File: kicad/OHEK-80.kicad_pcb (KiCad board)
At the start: 2 copper layers, 364.3 x 135.7 mm, 231 parts, among them J1 USB_C_Receptacle_USB2.0_16P, J2 Conn_01x04, J3 Conn_01x05, SW1 SW_Push, SW2 SW_Push, U1 AMS1117-3.3, U10 GH39FKSW, U11 GH39FKSW, U12 GH39FKSW, U13 GH39FKSW, U14 GH39FKSW, U15 GH39FKSW, U16 GH39FKSW, U17 GH39FKSW, U18 GH39FKSW, U19 GH39FKSW, U2 RP2040, U20 GH39FKSW, U21 GH39FKSW, U22 GH39FKSW, U23 GH39FKSW, U24 GH39FKSW, U25 GH39FKSW, U26 GH39FKSW, U27 GH39FKSW, U28 GH39FKSW, U29 GH39FKSW, U3 GH39FKSW, U30 GH39FKSW, U31 GH39FKSW, U32 GH39FKSW, U33 GH39FKSW, U34 GH39FKSW, U35 GH39FKSW, U36 GH39FKSW, U37 GH39FKSW, U38 GH39FKSW, U39 GH39FKSW, U4 GH39FKSW, U40 GH39FKSW, U41 GH39FKSW, U42 GH39FKSW, U43 GH39FKSW, U44 GH39FKSW, U45 GH39FKSW, U46 GH39FKSW, U47 GH39FKSW, U48 GH39FKSW, U49 GH39FKSW, U5 GH39FKSW, U50 GH39FKSW, U51 GH39FKSW, U52 GH39FKSW, U53 GH39FKSW, U54 GH39FKSW, U55 GH39FKSW, U56 GH39FKSW, U57 GH39FKSW, U58 GH39FKSW, U59 GH39FKSW, U6 GH39FKSW, U60 GH39FKSW, U61 GH39FKSW, U62 GH39FKSW, U63 GH39FKSW, U64 GH39FKSW, U65 GH39FKSW, U66 GH39FKSW, U67 GH39FKSW, U68 GH39FKSW, U69 GH39FKSW, U7 GH39FKSW, U70 GH39FKSW, U71 GH39FKSW, U72 GH39FKSW, U73 GH39FKSW, U74 GH39FKSW, U75 GH39FKSW, U76 GH39FKSW, U77 GH39FKSW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

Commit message: Removed J2 and cleaned up PCB a bit
I realized that daughterboard support is useless as Void Switches are entirely contactless so there is no use in gasket mounting the keyboard.
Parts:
- removed J2: Conn_01x04, Connector_JST:JST_PH_S4B-PH-K_1x04_P2.00mm_Horizontal
- moved F1 11.0 mm to (162.1, 101.7)
- moved R4 9.10 mm to (171.2, 99.0), turned to 0 degrees
- moved R5 6.63 mm to (171.2, 100.9), turned to 0 degrees
- moved SW2 3.67 mm to (179.7, 122.9), turned to 180 degrees
- moved C12 1.94 mm to (176.1, 118.4), turned to 180 degrees
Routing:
- net +3V3: track 288.6 -> 264.1 mm, vias 126 -> 123
- net GND: track 646.6 -> 626.1 mm
- net +5V: track 30.8 -> 16.1 mm, vias 2 -> 0
- net Net-(U2-USB_DM): track 17.1 -> 9.86 mm
- net Net-(U2-USB_DP): track 15.6 -> 9.83 mm
- net VBUS: track 22.4 -> 18.5 mm
- net D+: track 31.0 -> 28.5 mm
- net Net-(R7-Pad1): track 11.4 -> 10.6 mm
- net D-: track 27.7 -> 27.2 mm

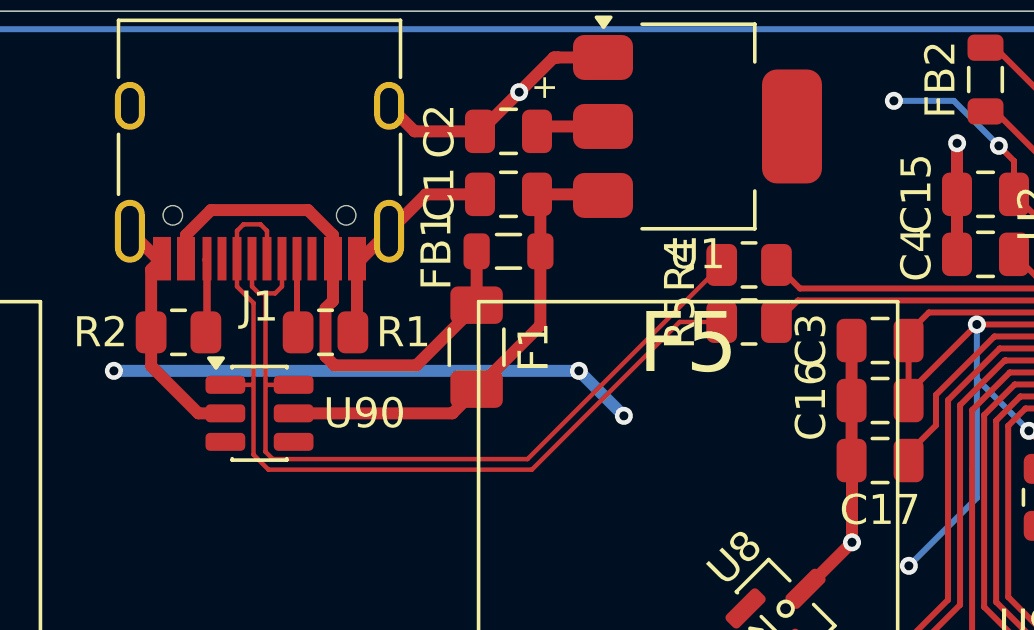
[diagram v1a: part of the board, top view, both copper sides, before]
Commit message: Fix issue where FB1 and F1 were in parallel
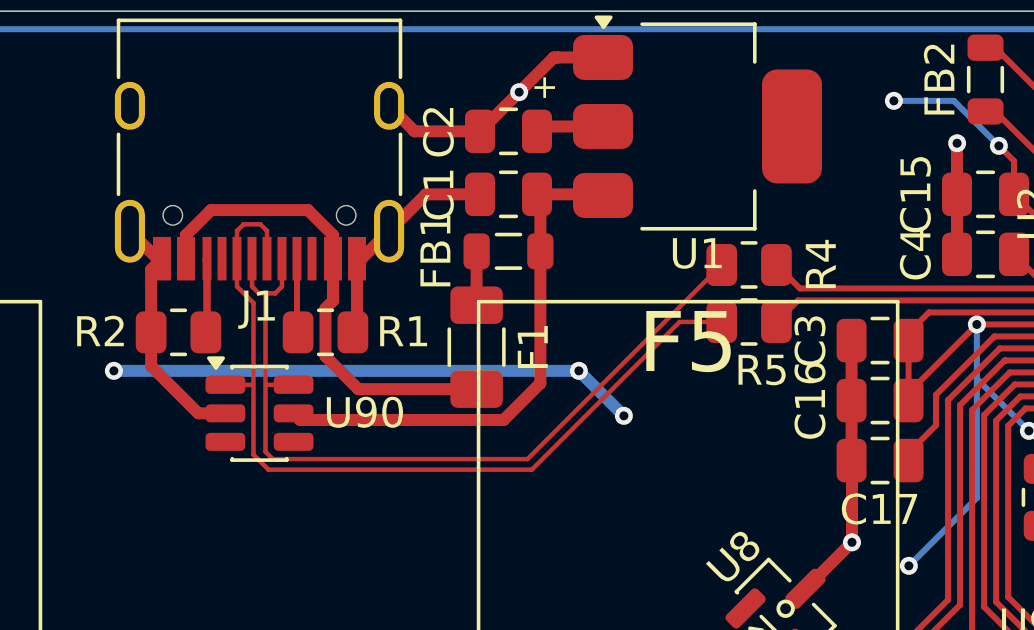
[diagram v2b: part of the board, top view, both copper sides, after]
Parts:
- C2: value 22u -> 22u Tantalum
- turned F1 to 90 degrees
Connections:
- F1 pad 2: +5V -> Net-(F1-Pad2)
- FB1 pad 1: VBUS -> Net-(F1-Pad2)
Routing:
- net VBUS: track 18.5 -> 16.2 mm
- net Net-(F1-Pad2): track 0.00 -> 1.80 mm
- net +5V: track 16.1 -> 17.4 mm

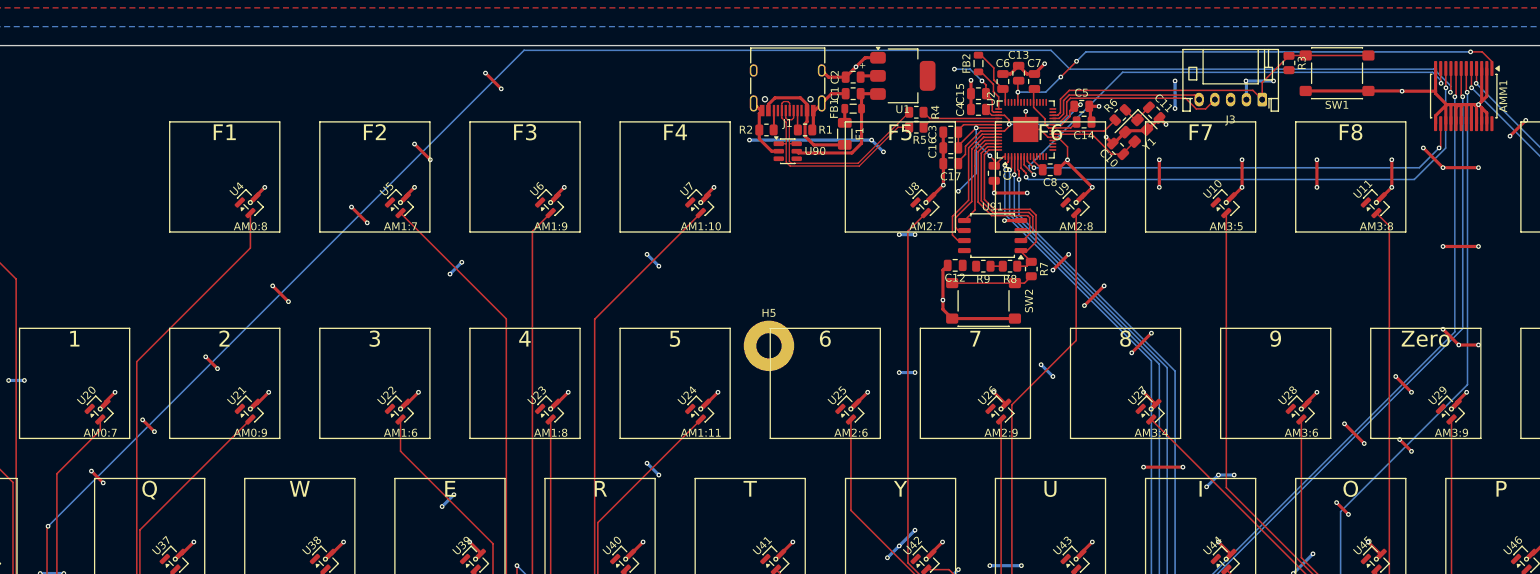
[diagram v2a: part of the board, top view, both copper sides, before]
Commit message: Fix incorrect footprints for SW1 and SW2
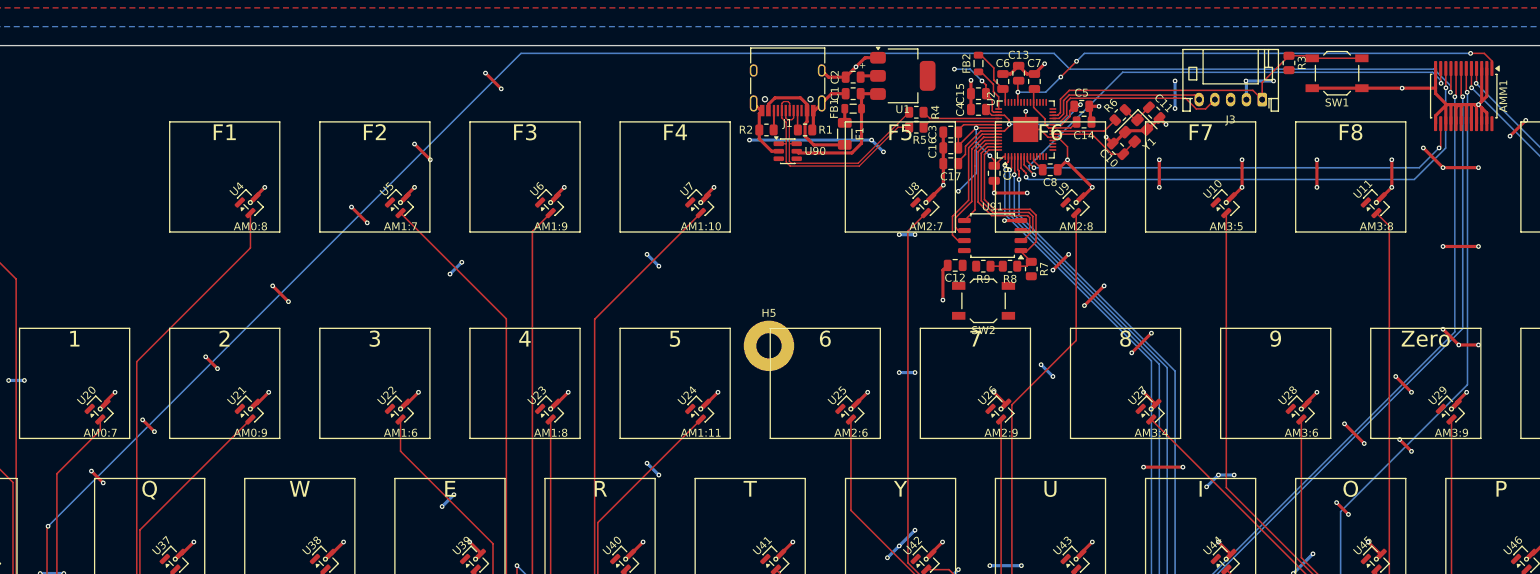
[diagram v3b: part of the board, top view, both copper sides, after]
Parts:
- SW1, SW2: footprint Button_Switch_SMD:SW_SPST_PTS645Sx43SMTR92 -> Button_Switch_SMD:SW_SPST_TL3342
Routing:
- net GND: track 626.1 -> 614.5 mm
- net Net-(R7-Pad1): track 10.6 -> 0.16 mm
- net RESET: track 46.4 -> 45.8 mm
